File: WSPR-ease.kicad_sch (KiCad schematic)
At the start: 77 parts, among them J101 GNSS Ant, J102 USB_C_16P_Stacked, J103 Tx Ant, Q101 MMBF170, Q102 MMBF170, Q103 MMBF170, Q104 MMBF170, Q105 MMBF170, Q106 MMBF170, Q107 MMBF170, Q108 MMBF170, Q109 MMBF170, Q110 MMBF170, Q111 MMBF170, Q112 MMBF170, SW101 BOOTSEL, SW102 RESET, T101 BN-43-202_DualPri_CTSec, U101 W25Q128JVS, U102 RP2040, U103 CD74AC244M, U104 ATGM336H-5N31, U105 NCP1117-3.3_SOT223, Y101 ABM8-272-T3

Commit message: Starting layout a bit
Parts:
- removed AE101: GPS_Patch_25mm, Library:gnss-antenna, symbol Library:GPS_Patch_25mm
- removed C109: 100nF, Capacitor_SMD:C_0603_1608Metric, symbol Device:C
- removed Q101, Q102, Q103, Q104, Q105, Q106, Q107, Q108, Q109, Q110, Q111, Q112: MMBF170, Package_TO_SOT_SMD:SOT-23, symbol Transistor_FET:BS170F
- removed R107, R108, R109, R111, R114, R115, R117, R118, R119: 10, Resistor_SMD:R_0603_1608Metric, symbol Device:R_US
- removed R116, R120: 0, Resistor_SMD:R_0603_1608Metric, symbol Device:R_US
- removed T101: BN-43-202_DualPri_CTSec, Library:bn-43-202-horizontal, symbol Library:Transformer_BN43_202_DualTap
- removed U103: CD74AC244M, DW20, symbol Library:CD74AC244M
- added C114: 100nF, Capacitor_SMD:C_0805_2012Metric, symbol Device:C
- added J101: DEBUG, Connector:Tag-Connect_TC2030-IDC-NL_2x03_P1.27mm_Vertical, symbol Connector:Conn_ARM_SWD_TagConnect_TC2030-NL
- added Q101: 2N7002, Package_TO_SOT_SMD:SOT-23, symbol Transistor_FET:2N7002
- C107: footprint Capacitor_SMD:C_0805_2012Metric -> Capacitor_SMD:C_0603_1608Metric
- C121: renamed from C119; now fitted
- J102: renamed from J101; now fitted
- L101: now fitted
- R110: value 10 -> 200
- R112: value 10 -> 200k
- R113: value 10 -> 100k
- Y101: value ABM8-272-T3 -> 12MHz
- renumbered C110 to C109, C111 to C110, C112 to C111, C113 to C112, C116 to C113, C120 to C115, C114 to C116, C115 to C117, C117 to C118, C123 to C119, C118 to C120, C121 to C122, C122 to C123, J102 to J103, J103 to J104, R121 to R101, R122 to R102, R101 to R103, R102 to R104, R125 to R105, R126 to R106, R103 to R107, R104 to R108, R105 to R109, R106 to R111, R123 to R114, R124 to R115, U105 to U103
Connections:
- net +3.3V: now also C107.1, R110.1, J101.1 (VCC), Q101.1 (G); no longer C107.2, C110.1, U102.43 (ADC_AVDD), U102.44 (VREG_IN)
- net GND: now also C107.2, R113.2, C114.2, J101.5 (GND); no longer C107.1
- net VBUS: now also R112.1
- net at R112.2: now also R113.1, C114.1, Q101.2 (S)
- net nRESET: now reaches R103.2, SW102.2, U102.26 (RUN)
- net nRESET: now also J101.3 (~{RESET})
- net at C121.1: now also U104.11 (RF_IN)
- net at R110.2: now also U102.43 (ADC_AVDD)
- net SWCLK: now reaches U102.24 (SWCLK)
- net SWCLK: now also J101.4 (SWCLK)
- net SWD: now reaches U102.25 (SWD)
- net SWD: now also J101.2 (SWDIO)
- net ethMISO: now reaches U102.27 (GPIO16)
- net ethNCS: now reaches U102.28 (GPIO17)
- net ethSCLK: now reaches U102.29 (GPIO18)
- net ethMOSI: now reaches U102.30 (GPIO19)
- net ethNIRQ: now reaches U102.31 (GPIO20)
- net ethRESET: now reaches U102.32 (GPIO21)
- net at U102.41 (GPIO29_ADC3): now also Q101.3 (D)
- new net: C110.1, U102.44 (VREG_IN)
- no-connect marks 5 -> 17
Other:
- added sheet Ethernet (ether.kicad_sch)
- added sheet Transmitter (tx.kicad_sch)
- moved on the sheet: BT101, C104, C108, C109, C111, C112, C113, C115, C116, C117, C118, C119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

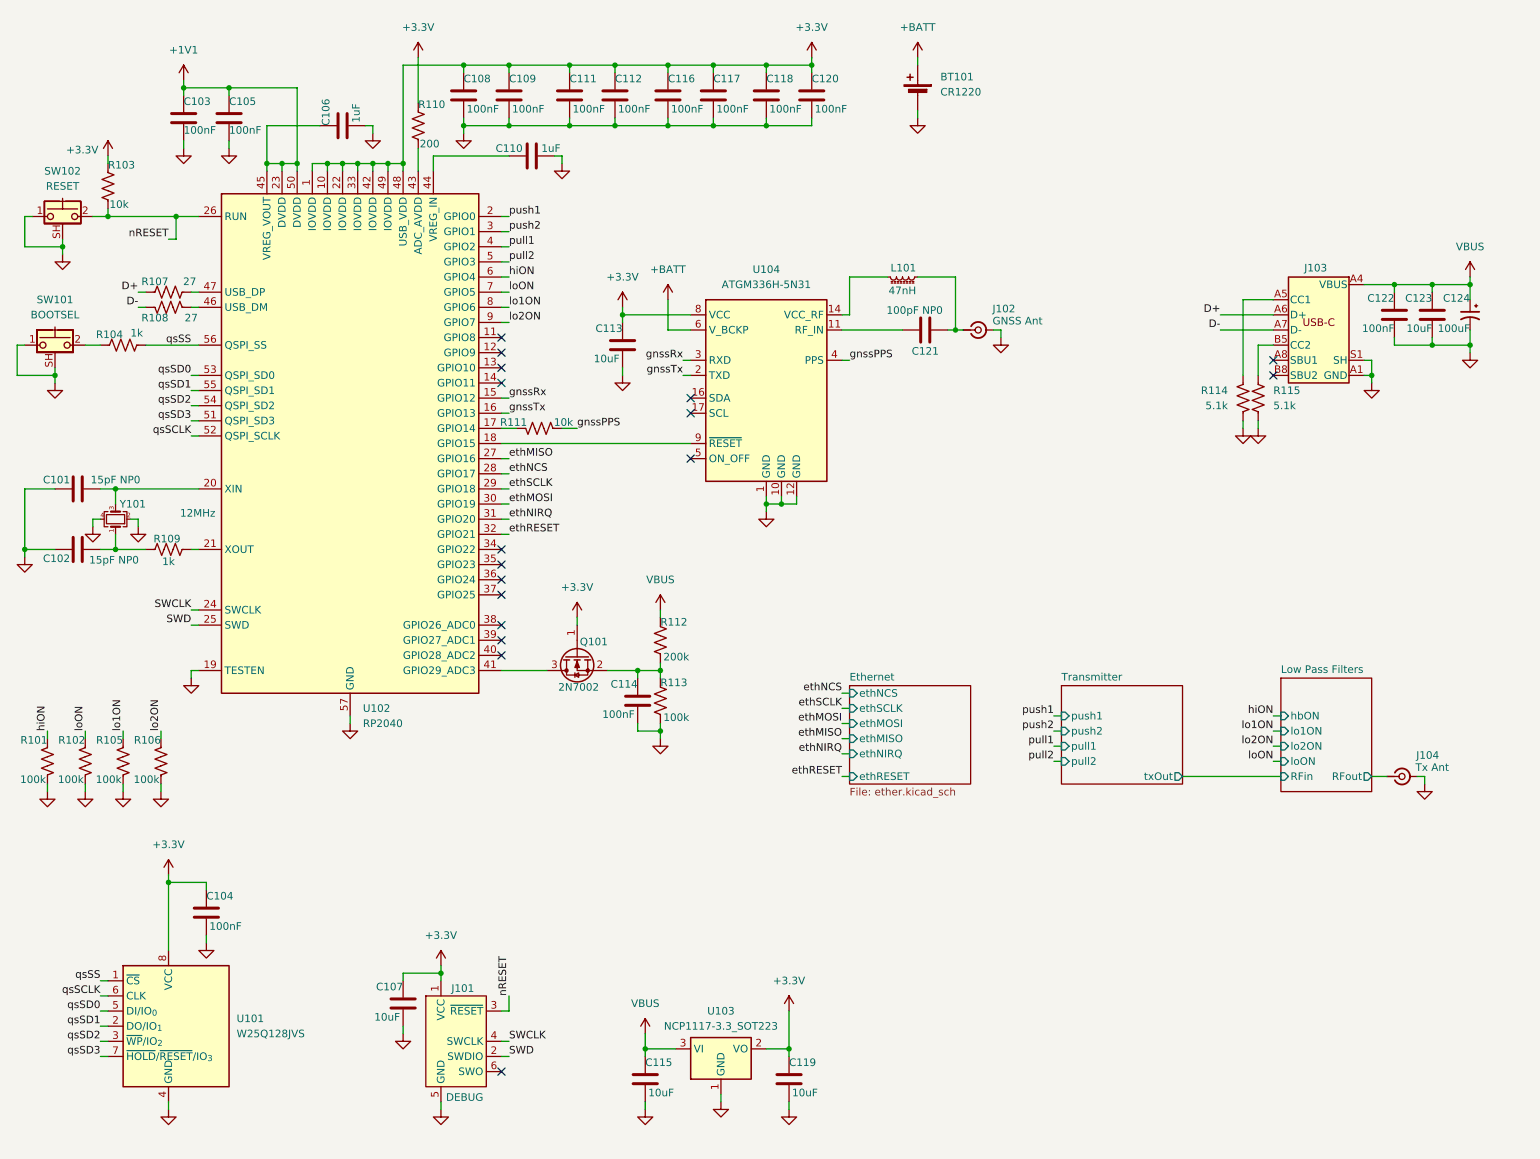
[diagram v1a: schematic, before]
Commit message: Fix filters for proper response. Now we have FPGA + ESP32S3.
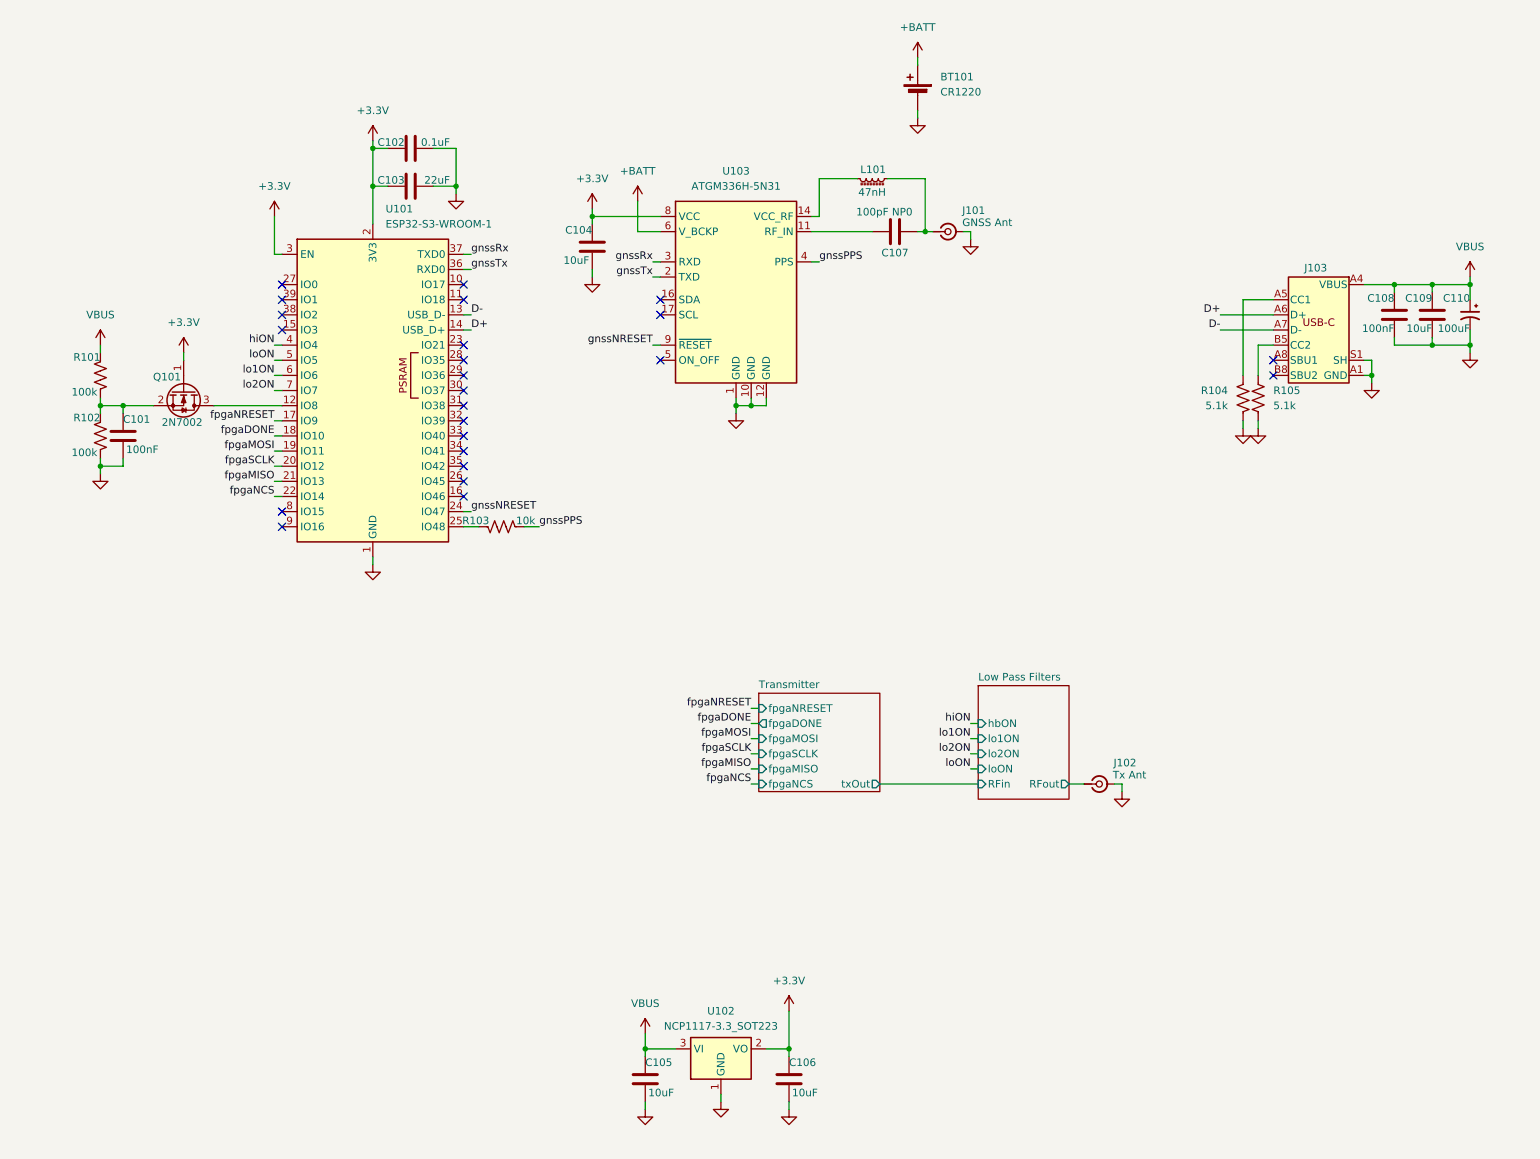
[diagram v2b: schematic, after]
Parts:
- removed C104, C105, C108, C109, C111, C112, C116, C117, C118, C120: 100nF, Capacitor_SMD:C_0603_1608Metric, symbol Device:C
- removed C106, C110: 1uF, Capacitor_SMD:C_0603_1608Metric, symbol Device:C
- removed C107: 10uF, Capacitor_SMD:C_0603_1608Metric, symbol Device:C
- removed C114: 100nF, Capacitor_SMD:C_0805_2012Metric, symbol Device:C
- removed J101: DEBUG, Connector:Tag-Connect_TC2030-IDC-NL_2x03_P1.27mm_Vertical, symbol Connector:Conn_ARM_SWD_TagConnect_TC2030-NL
- removed R104, R109: 1k, Resistor_SMD:R_0603_1608Metric, symbol Device:R_US
- removed R105, R106, R113: 100k, Resistor_SMD:R_0603_1608Metric, symbol Device:R_US
- removed R107, R108: 27, Resistor_SMD:R_0603_1608Metric, symbol Device:R_US
- removed R110: 200, Resistor_SMD:R_0603_1608Metric, symbol Device:R_US
- removed R111: 10k, Resistor_SMD:R_0603_1608Metric, symbol Device:R_US
- removed R112: 200k, Resistor_SMD:R_0603_1608Metric, symbol Device:R_US
- removed SW101: BOOTSEL, Button_Switch_SMD:SW_SPST_CK_KMS2xxGP, symbol Switch:CK_KMS2xxG
- removed SW102: RESET, Button_Switch_SMD:SW_SPST_CK_KMS2xxGP, symbol Switch:CK_KMS2xxG
- removed U101: W25Q128JVS, Package_SO:SOIC-8_5.3x5.3mm_P1.27mm, symbol Memory_Flash:W25Q128JVS
- removed U102: RP2040, Package_DFN_QFN:QFN-56-1EP_7x7mm_P0.4mm_EP3.2x3.2mm, symbol Library:RP2040
- removed Y101: 12MHz, Crystal:Crystal_SMD_Abracon_ABM8G-4Pin_3.2x2.5mm, symbol Device:Crystal_GND24_Small
- added U101: ESP32-S3-WROOM-1, RF_Module:ESP32-S3-WROOM-1, symbol RF_Module:ESP32-S3-WROOM-1
- C101: value 15pF NP0 -> 100nF; footprint Capacitor_SMD:C_0603_1608Metric -> Capacitor_SMD:C_0805_2012Metric
- C102: value 15pF NP0 -> 0.1uF
- C103: value 100nF -> 22uF
- renumbered C113 to C104, C115 to C105, C119 to C106, C121 to C107, C122 to C108, C123 to C109, C124 to C110, J102 to J101, J104 to J102, R114 to R104, R115 to R105, U103 to U102, U104 to U103
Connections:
- net +1V1 is gone; now on net +3.3V: C103.1
- net nRESET is gone; now on net gnssPPS: R103.2
- net +3.3V: now also C102.1, U101.2 (3V3), U101.3 (EN); no longer R103.1
- net D+: now also U101.14 (USB_D+)
- net D-: now also U101.13 (USB_D-)
- net GND: now also C101.2, C102.2, U101.1 (GND), U101.40 (GND), U101.41 (GND); no longer C101.1, C102.1, R101.2
- net VBUS: now also R101.1
- net gnssRx: now also U101.37 (TXD0)
- net gnssTx: now also U101.36 (RXD0)
- net hiON: now also U101.4 (IO4); no longer R101.1
- net lo1ON: now also U101.6 (IO6)
- net lo2ON: now also U101.7 (IO7)
- net loON: now also U101.5 (IO5); no longer R102.1
- net at Q101.2 (S): now also C101.1, R101.2, R102.1
- net at Q101.3 (D): now also U101.12 (IO8)
- net gnssNRESET: now reaches U103.9 (~{RESET})
- net gnssNRESET: now also U101.24 (IO47)
- new net: R103.1, U101.25 (IO48)
- new net fpgaDONE: U101.18 (IO10)
- new net fpgaMISO: U101.21 (IO13)
- new net fpgaMOSI: U101.19 (IO11)
- new net fpgaNCS: U101.22 (IO14)
- new net fpgaNRESET: U101.17 (IO9)
- new net fpgaSCLK: U101.20 (IO12)
- no-connect marks 17 -> 24
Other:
- removed sheet Ethernet
- sheet Transmitter ports: added fpgaDONE, fpgaMISO, fpgaMOSI, fpgaNCS, fpgaNRESET, fpgaSCLK; removed pull1, pull2, push1, push2
- moved on the sheet: C104, C107, J101, J102, L101, U103

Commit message: Well it is routed and passes DRC
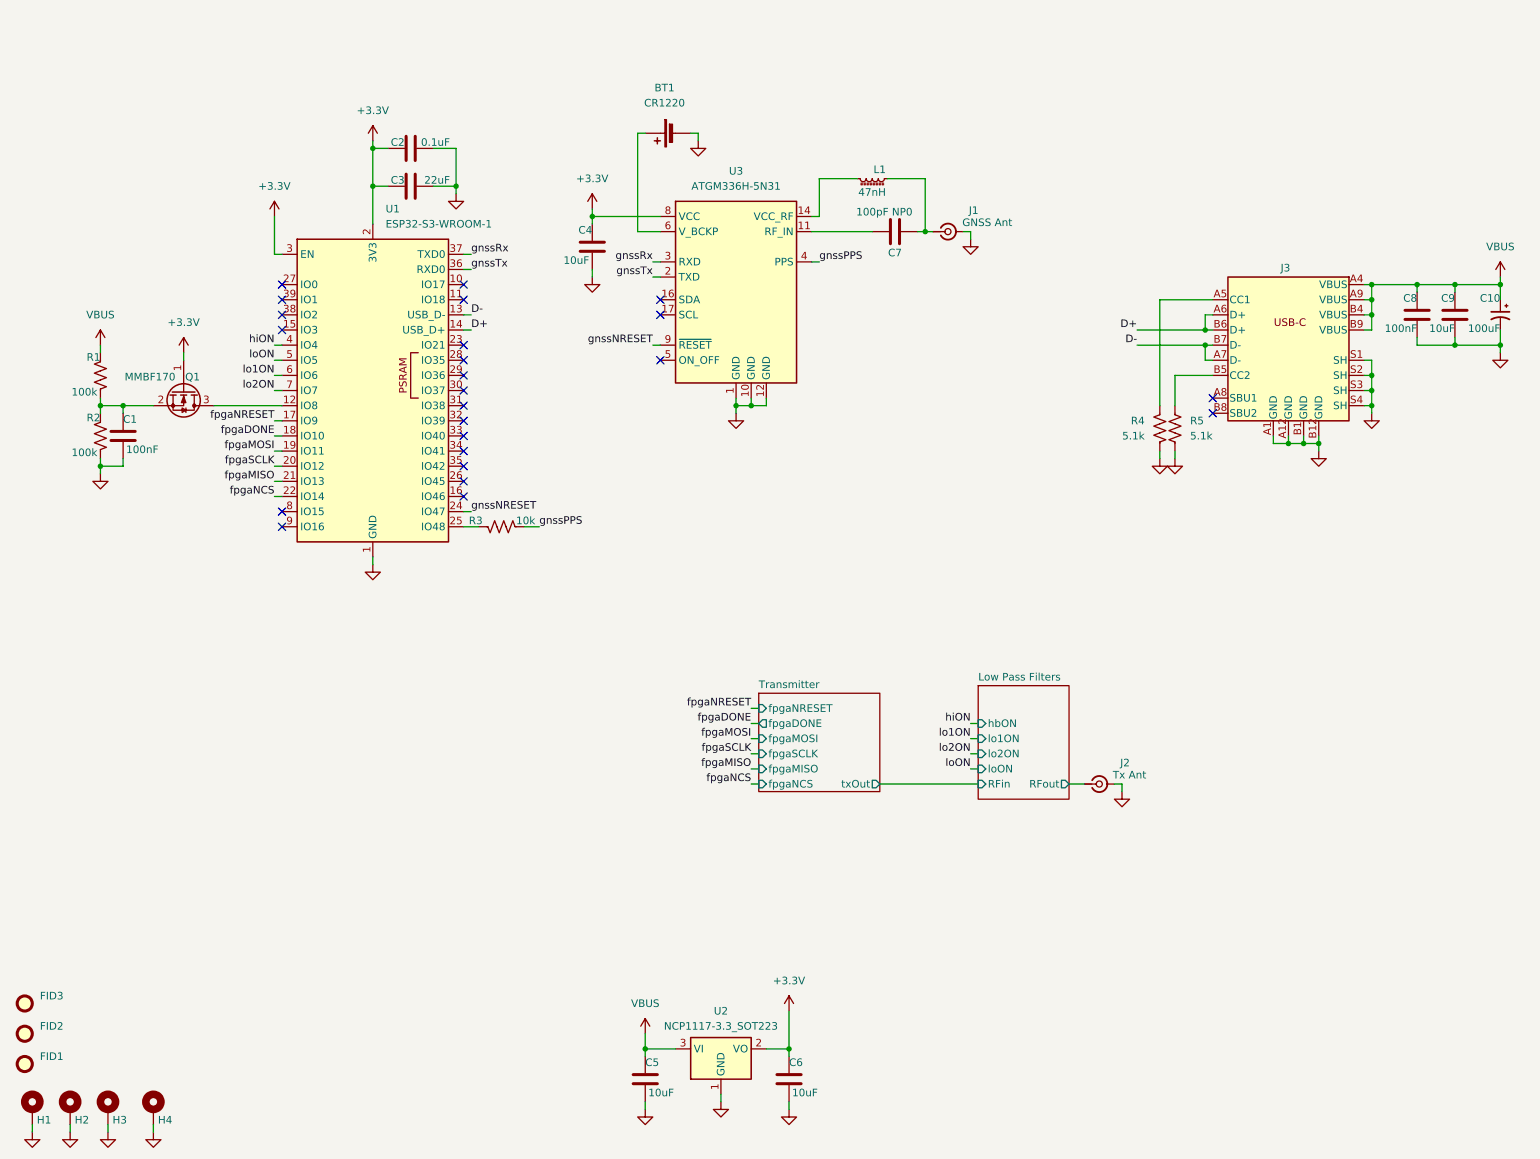
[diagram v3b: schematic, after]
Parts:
- removed Q101: 2N7002, Package_TO_SOT_SMD:SOT-23, symbol Transistor_FET:2N7002
- added FID1, FID2, FID3: Fiducial, Fiducial:Fiducial_1mm_Mask2mm, symbol Mechanical:Fiducial
- added H1, H2, H3, H4: MountingHole_Pad, MountingHole:MountingHole_3.2mm_M3_ISO7380_Pad, symbol Mechanical:MountingHole_Pad
- added Q1: MMBF170, Package_TO_SOT_SMD:SOT-23, symbol Transistor_FET:BS170F
- C10: renamed from C110; footprint Capacitor_SMD:C_1206_3216Metric -> Capacitor_SMD:CP_Elec_8x10.5; LCSC (none) -> C1849748; MFG (none) -> Vishay; MPN (none) -> MAL215097011E3
- U1: renamed from U101; footprint RF_Module:ESP32-S3-WROOM-1 -> Library:ESP32-S3-WROOM-1
- renumbered BT101 to BT1, C101 to C1, C102 to C2, C103 to C3, C104 to C4, C105 to C5, C106 to C6, C107 to C7, C108 to C8, C109 to C9, J101 to J1, J102 to J2, J103 to J3, L101 to L1, R101 to R1, R102 to R2, R103 to R3, R104 to R4, R105 to R5, U102 to U2, U103 to U3
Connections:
- net +3.3V: now also Q1.1 (G)
- net GND: now also H1.1, H2.1, H3.1, H4.1
- net at C1.1, R1.2, R2.1: now also Q1.2 (S)
- net at U1.12 (IO8): now also Q1.3 (D)
- net +BATT: no longer names the net of BT1.1 (+), U3.6 (V_BCKP)
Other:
- moved on the sheet: BT1, C10, C8, C9, R4, R5
